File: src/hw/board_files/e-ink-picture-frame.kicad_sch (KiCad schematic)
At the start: 3 parts, among them J1 USB_C_Receptacle_USB2.0_14P, J2 Micro_SD_Card, U1 ESP32-S3-WROOM-1

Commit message: Sch progress
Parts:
- removed J2: Micro_SD_Card, symbol Connector:Micro_SD_Card
- removed U1: ESP32-S3-WROOM-1, RF_Module:ESP32-S3-WROOM-1, symbol RF_Module:ESP32-S3-WROOM-1
- added BT1: Battery_Cell, symbol Device:Battery_Cell
- added C1, C2, C3: 10u, Capacitor_SMD:C_0805_2012Metric_Pad1.18x1.45mm_HandSolder, symbol Device:C_Small
- added C6: 100n, Capacitor_SMD:C_0603_1608Metric_Pad1.08x0.95mm_HandSolder, symbol Device:C_Small
- added D1, D2, D3: LED, LED_SMD:LED_0805_2012Metric_Pad1.15x1.40mm_HandSolder, symbol Device:LED
- added J3: Molex 104031-0811, Connector_Card:microSD_HC_Molex_104031-0811, symbol Connector:Micro_SD_Card_Det1
- added R1: 1k3, Resistor_SMD:R_0603_1608Metric_Pad0.98x0.95mm_HandSolder, symbol Device:R_US
- added R14, R15, R16, R17, R2: 10k, Resistor_SMD:R_0603_1608Metric_Pad0.98x0.95mm_HandSolder, symbol Device:R_US
- added R3, R4, R7: 1k, Resistor_SMD:R_0603_1608Metric_Pad0.98x0.95mm_HandSolder, symbol Device:R_US
- added R5, R6: 27R, symbol Device:R_Small_US
- added R8, R9: 5k1, symbol Device:R_Small_US
- added U1: MCP73871, Package_DFN_QFN:QFN-20-1EP_4x4mm_P0.5mm_EP2.5x2.5mm, symbol Battery_Management:MCP73871
- added U2: USBLC6-2SC6, Package_TO_SOT_SMD:SOT-23-6, symbol Power_Protection:USBLC6-2SC6
- J1: footprint (none) -> Connector_USB:USB_C_Receptacle_GCT_USB4105-xx-A_16P_TopMnt_Horizontal
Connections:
- net GND: now reaches J1.A1 (GND), J1.A12 (GND), J1.B1 (GND), J1.B12 (GND)
- net GND: now also J1.S1 (SHIELD), BT1.2 (-), C1.1, C2.2, C3.2, C6.2, J3.10 (SHIELD), J3.6 (VSS), R1.1, R2.1, R8.2, R9.2, U1.10 (V_{SS}), U1.11 (V_{SS}), U1.21 (V_{SS}), U1.3 (SEL), U1.9 (~{TE}), U2.2 (GND)
- net VBUS: now reaches J1.A4 (VBUS), J1.A9 (VBUS), J1.B4 (VBUS), J1.B9 (VBUS)
- net VBUS: now also C1.2, D1.2 (A), D2.2 (A), D3.2 (A), U1.17 (CE), U1.18 (IN), U1.19 (IN), U1.2 (VPCC), U1.4 (PROG2), U2.5 (VBUS)
- net at J1.A5 (CC1): now also R9.1
- net at J1.A6 (D+): now also J1.B6 (D+), U2.3 (I/O2)
- net at J1.A7 (D-): now also J1.B7 (D-), U2.1 (I/O1)
- net at J1.B5 (CC2): now also R8.1
- new net: R3.1, U1.6 (~{PG})
- new net: D1.1 (K), R3.2
- new net: R6.2, U2.4 (I/O2)
- new net: R5.1, U2.6 (I/O1)
- new net: R2.2, U1.12 (PROG3)
- new net: D2.1 (K), R4.2
- new net: R4.1, U1.8 (STAT1/~{LBO})
- new net: R7.1, U1.7 (STAT2)
- new net: D3.1 (K), R7.2
- new net: R1.2, U1.13 (PROG1)
- new net +3V3: C6.1, J3.4 (VDD), R14.1, R15.1, R16.1, R17.1
- new net NTC_THERM: U1.5 (THERM)
- new net SD_CS: J3.2 (DAT3/CD), R14.2
- new net SPI_MISO: J3.7 (DAT0), R17.2
- new net SPI_MOSI: J3.3 (CMD), R15.2
- new net SPI_SCK: J3.5 (CLK), R16.2
- new net USB_D+: R6.1
- new net USB_D-: R5.2
- new net VBAT: BT1.1 (+), C3.1, U1.14 (V_{BAT}), U1.15 (V_{BAT}), U1.16 (V_{BAT_SENSE})
- new net V_SYS: C2.1, U1.1 (OUT), U1.20 (OUT)
- no-connect marks 0 -> 3
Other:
- added sheet Microcontroller (microcontroller.kicad_sch)
- note added: "E-Ink Picture Frame"
- note added: "LDO: Richtek RT9080-33GJ5"
- note added: "MicroSD Card"
- moved on the sheet: J1

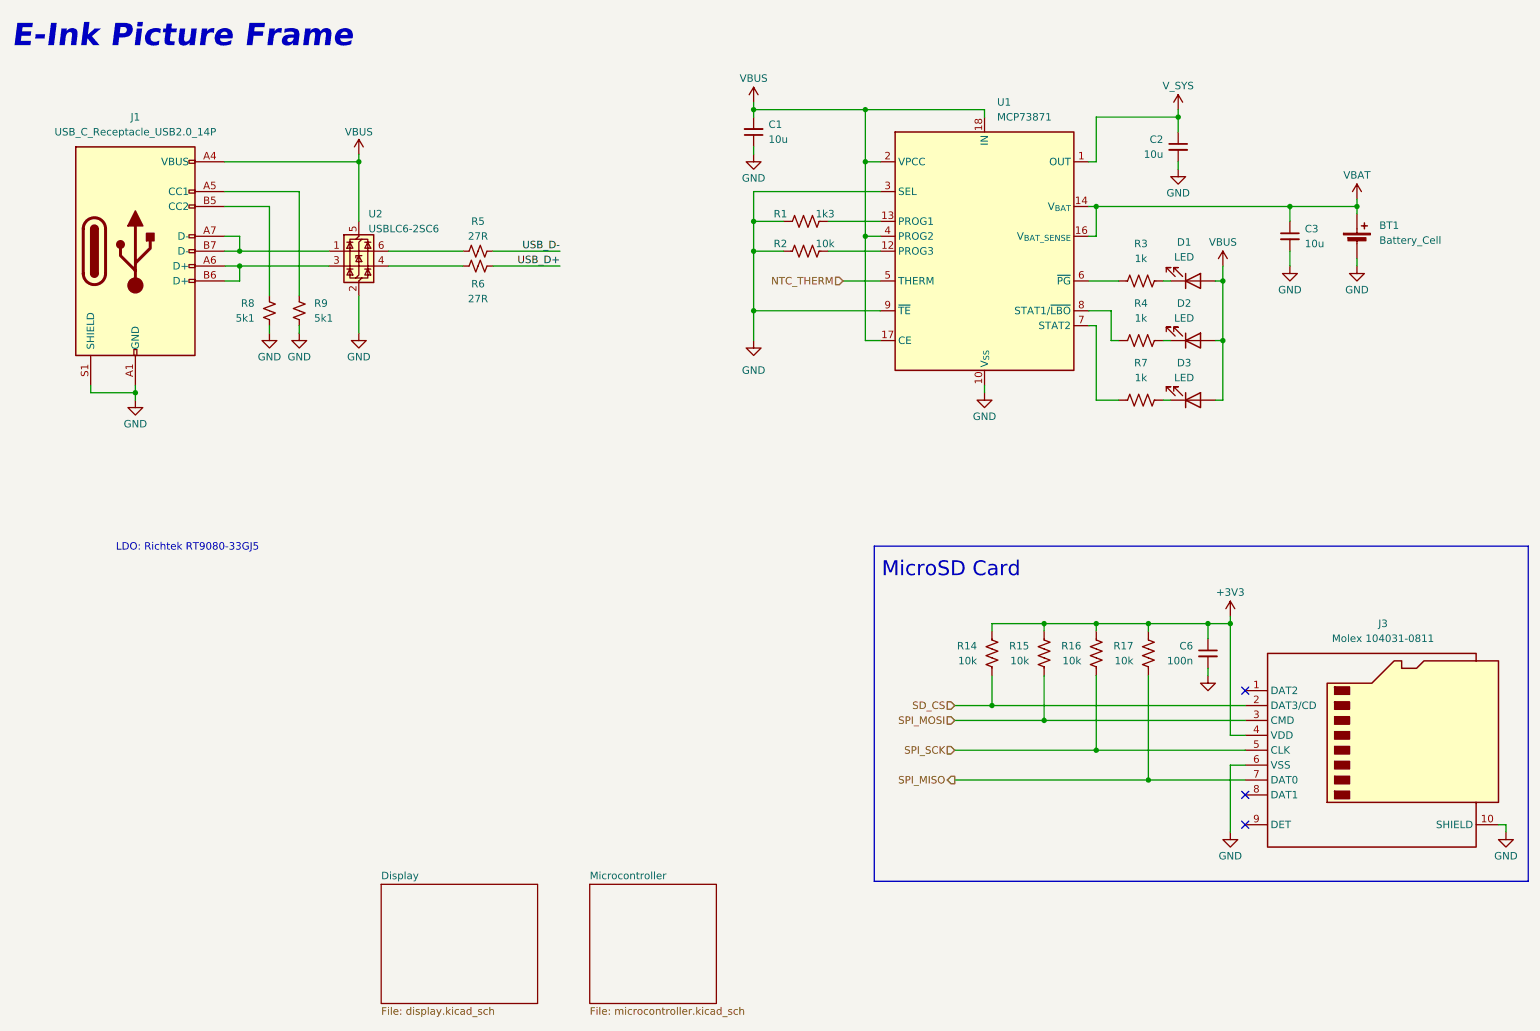
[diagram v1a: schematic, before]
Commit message: Schematic almost done. Assigning footprints
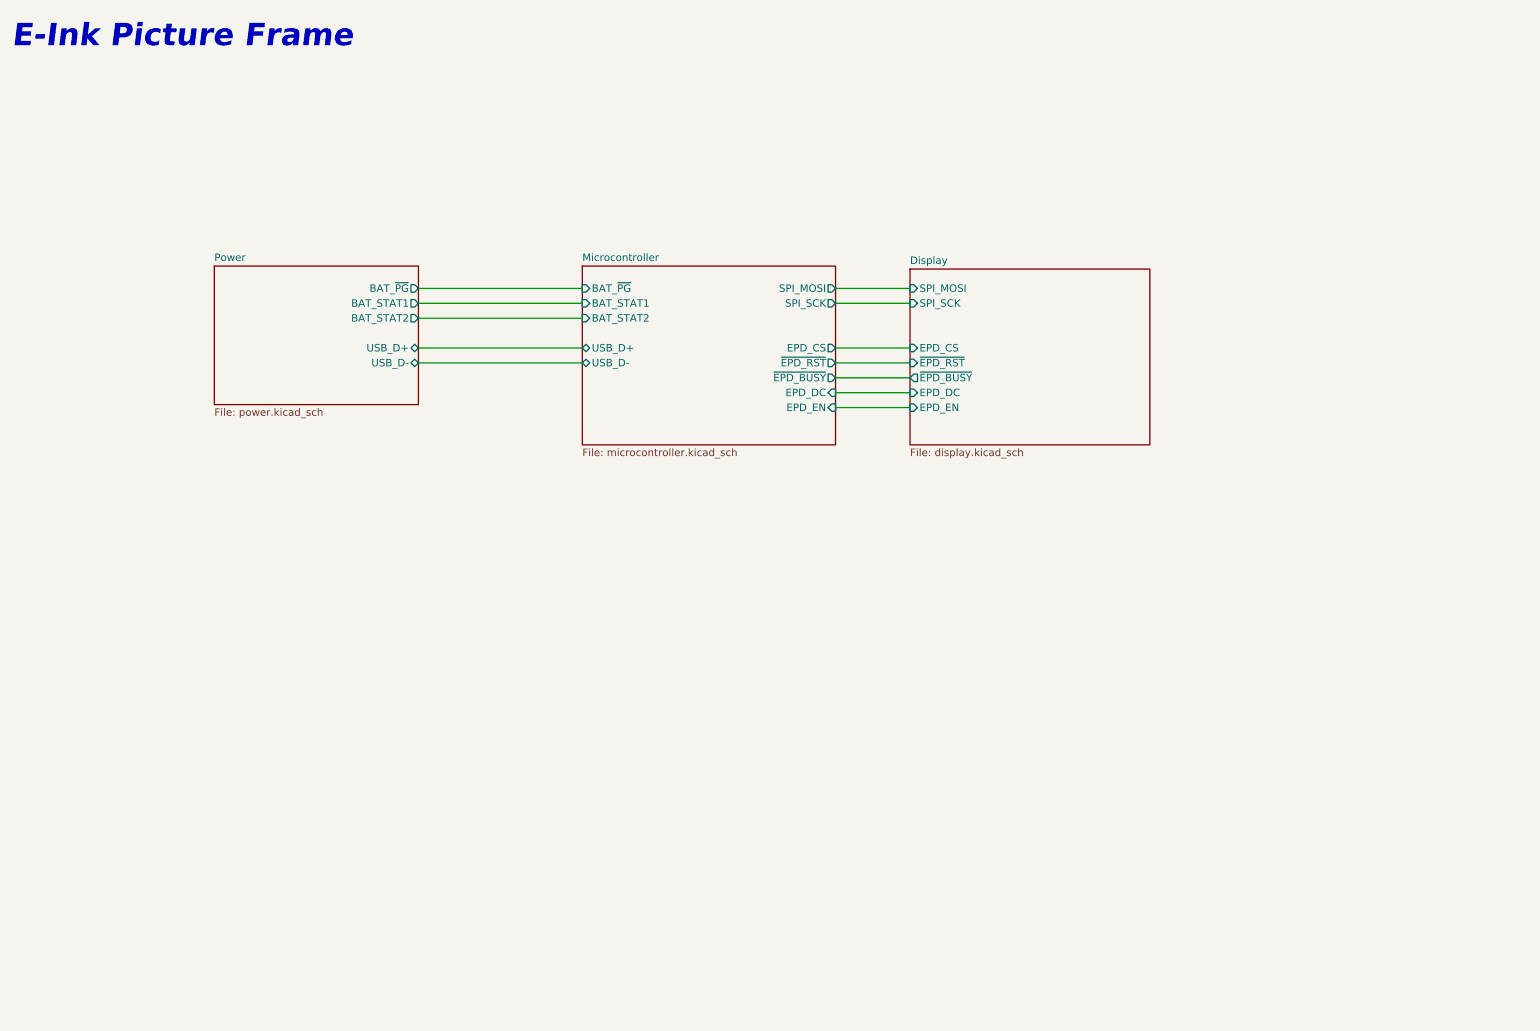
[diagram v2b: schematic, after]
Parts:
- removed BT1: Battery_Cell, symbol Device:Battery_Cell
- removed C1, C2, C3: 10u, Capacitor_SMD:C_0805_2012Metric_Pad1.18x1.45mm_HandSolder, symbol Device:C_Small
- removed C6: 100n, Capacitor_SMD:C_0603_1608Metric_Pad1.08x0.95mm_HandSolder, symbol Device:C_Small
- removed D1, D2, D3: LED, LED_SMD:LED_0805_2012Metric_Pad1.15x1.40mm_HandSolder, symbol Device:LED
- removed J1: USB_C_Receptacle_USB2.0_14P, Connector_USB:USB_C_Receptacle_GCT_USB4105-xx-A_16P_TopMnt_Horizontal, symbol Connector:USB_C_Receptacle_USB2.0_14P
- removed J3: Molex 104031-0811, Connector_Card:microSD_HC_Molex_104031-0811, symbol Connector:Micro_SD_Card_Det1
- removed R1: 1k3, Resistor_SMD:R_0603_1608Metric_Pad0.98x0.95mm_HandSolder, symbol Device:R_US
- removed R14, R15, R16, R17, R2: 10k, Resistor_SMD:R_0603_1608Metric_Pad0.98x0.95mm_HandSolder, symbol Device:R_US
- removed R3, R4, R7: 1k, Resistor_SMD:R_0603_1608Metric_Pad0.98x0.95mm_HandSolder, symbol Device:R_US
- removed R5, R6: 27R, symbol Device:R_Small_US
- removed R8, R9: 5k1, symbol Device:R_Small_US
- removed U1: MCP73871, Package_DFN_QFN:QFN-20-1EP_4x4mm_P0.5mm_EP2.5x2.5mm, symbol Battery_Management:MCP73871
- removed U2: USBLC6-2SC6, Package_TO_SOT_SMD:SOT-23-6, symbol Power_Protection:USBLC6-2SC6
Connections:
- no-connect marks 3 -> 0
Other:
- added sheet Power (power.kicad_sch)
- sheet Display ports: added EPD_CS, EPD_DC, EPD_EN, SPI_MOSI, SPI_SCK, ~{EPD_BUSY}, ~{EPD_RST}; removed none
- sheet Microcontroller ports: added BAT_STAT1, BAT_STAT2, BAT_~{PG}, EPD_CS, EPD_DC, EPD_EN, SPI_MOSI, SPI_SCK, USB_D+, USB_D-, ~{EPD_BUSY}, ~{EPD_RST}; removed none
- note removed: "LDO: Richtek RT9080-33GJ5"
- note removed: "MicroSD Card"
